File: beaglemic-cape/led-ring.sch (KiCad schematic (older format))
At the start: 42 parts, among them U1 74HC595, U2 74HC595, U3 AMS1117

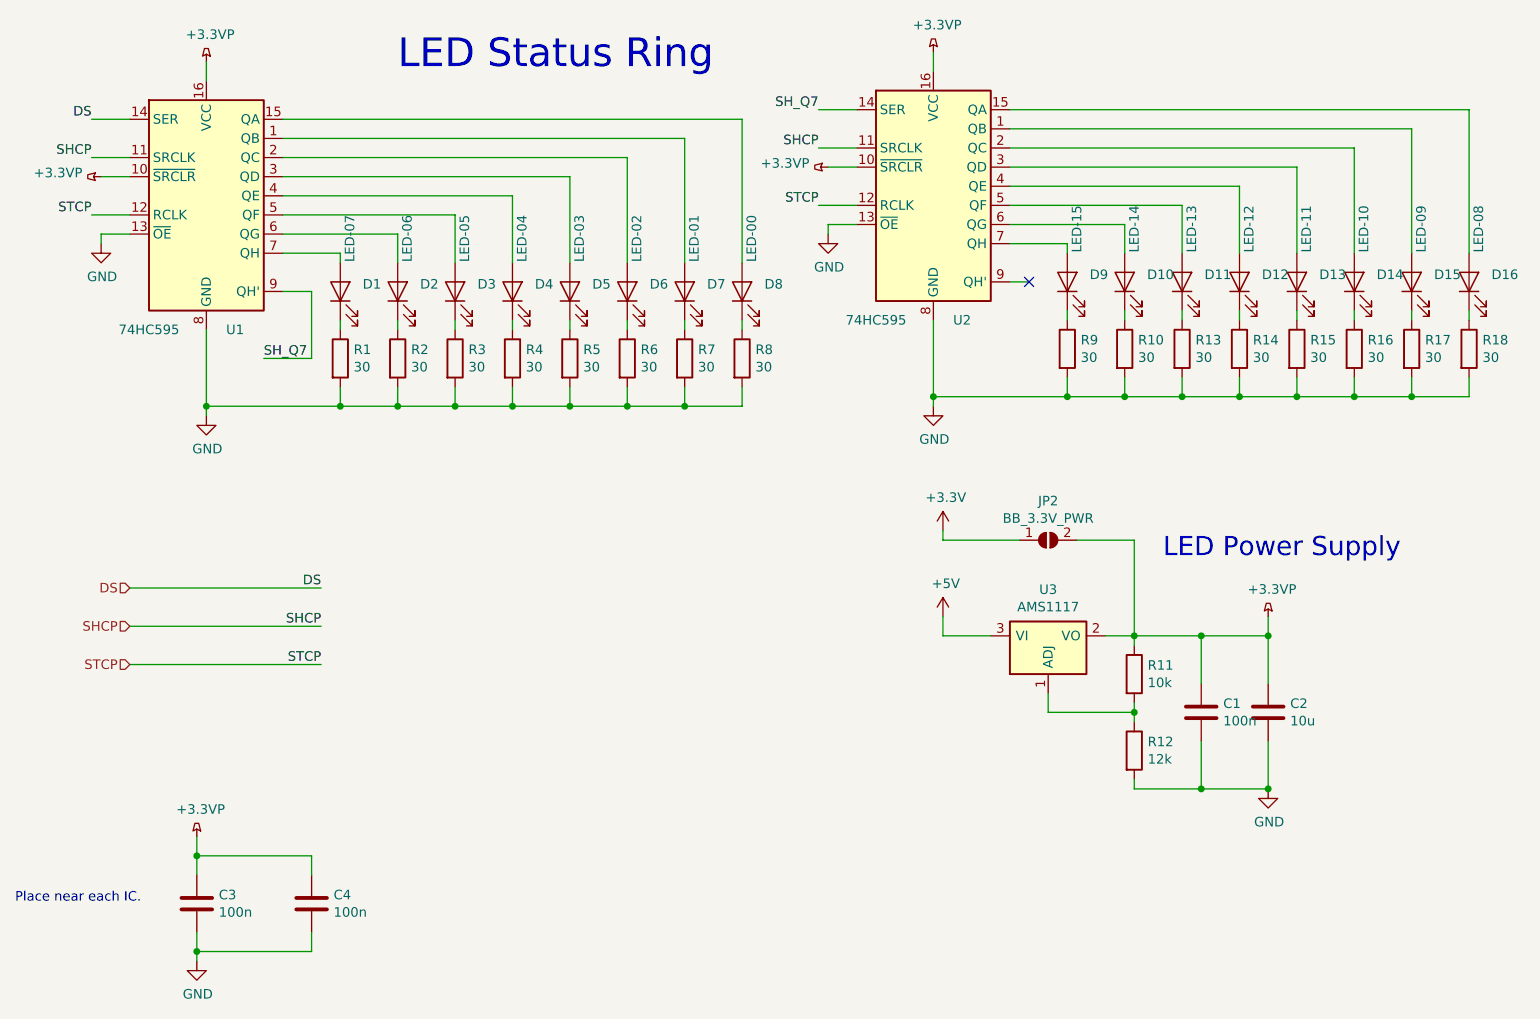
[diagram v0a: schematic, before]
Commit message: beaglemic-cape: Shrink PCB to 100x100mm
Let's keep the PCB in the hobby price range.

Version 1.0-rc2

TODO: Route me!

Signed-off-by: Dimitar Dimitrov <dimitar@dinux.eu>
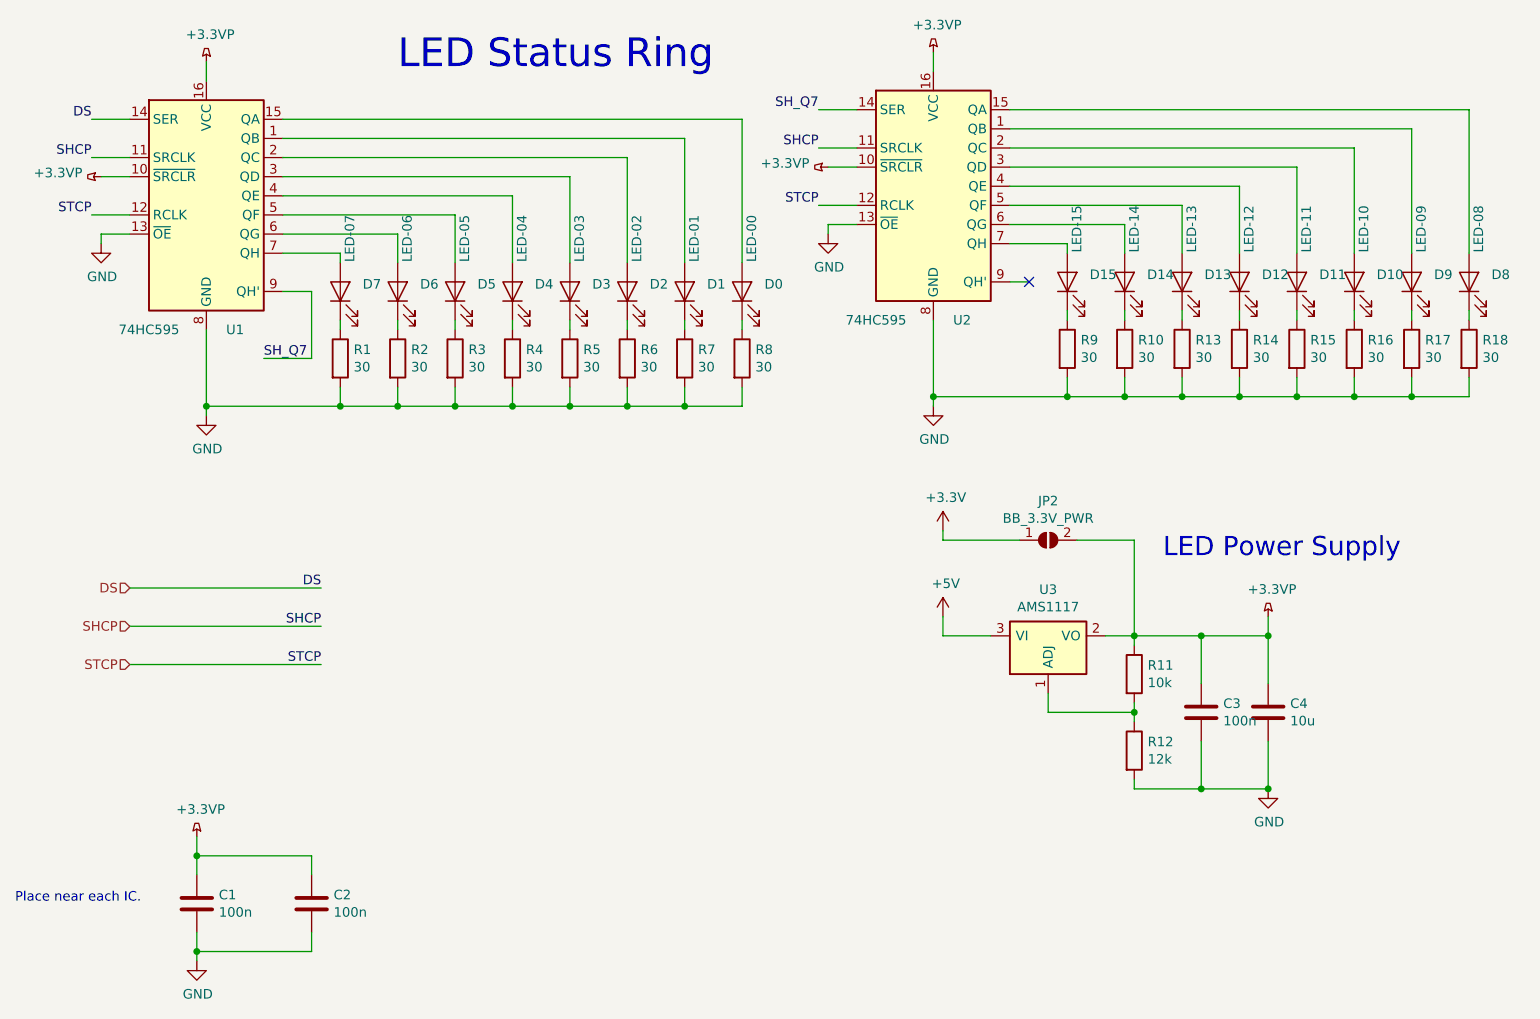
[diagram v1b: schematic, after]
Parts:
- renumbered C3 to C1, C4 to C2, C1 to C3, C2 to C4, D8 to D0, D7 to D1, D14 to D10, D13 to D11, D11 to D13, D10 to D14, D9 to D15, D6 to D2, D5 to D3, D3 to D5, D2 to D6, D1 to D7, D16 to D8, D15 to D9
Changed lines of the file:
@@
 Sheet 2 3
 Title "LED Ring"
-Date "2020-01-04"
-Rev "1.0-rc1"
+Date "2020-01-19"
+Rev "1.0-rc2"
 Comp "dimitar@dinux.eu"
 Comment1 "WARNING - NOT YET VALIDATED!"
@@
 $EndComp
 $Comp
-L power:GND #PWR046
+L power:GND #PWR049
 U 1 1 5E16CB08
 P 7650 5050
-F 0 "#PWR046" H 7650 4800 50  0001 C CNN
+F 0 "#PWR049" H 7650 4800 50  0001 C CNN
 F 1 "GND" H 7655 4877 50  0000 C CNN
 F 2 "" H 7650 5050 50  0001 C CNN
@@
 $EndComp
 $Comp
-L power:+3.3VP #PWR045
+L power:+3.3VP #PWR048
 U 1 1 5E16CB0E
 P 7650 4150
-F 0 "#PWR045" H 7800 4100 50  0001 C CNN
+F 0 "#PWR048" H 7800 4100 50  0001 C CNN
 F 1 "+3.3VP" H 7670 4293 50  0000 C CNN
 F 2 "" H 7650 4150 50  0001 C CNN
@@
 $EndComp
 $Comp
-L power:+5V #PWR044
+L power:+5V #PWR047
 U 1 1 5E16CB14
 P 5950 4150
-F 0 "#PWR044" H 5950 4000 50  0001 C CNN
+F 0 "#PWR047" H 5950 4000 50  0001 C CNN
 F 1 "+5V" H 5965 4323 50  0000 C CNN
 F 2 "" H 5950 4150 50  0001 C CNN
@@
 $EndComp
 $Comp
-L power:+3.3V #PWR043
+L power:+3.3V #PWR046
 U 1 1 5E16CB1A
 P 5950 3700
-F 0 "#PWR043" H 5950 3550 50  0001 C CNN
+F 0 "#PWR046" H 5950 3550 50  0001 C CNN
 F 1 "+3.3V" H 5965 3873 50  0000 C CNN
 F 2 "" H 5950 3700 50  0001 C CNN
@@
 	6950 4650 6950 4700
 $Comp
-L power:+3.3VP #PWR037
+L power:+3.3VP #PWR040
 U 1 1 5E16CB2E
 P 2100 1250
-F 0 "#PWR037" H 2250 1200 50  0001 C CNN
+F 0 "#PWR040" H 2250 1200 50  0001 C CNN
 F 1 "+3.3VP" H 2120 1393 50  0000 C CNN
 F 2 "" H 2100 1250 50  0001 C CNN
@@
 $EndComp
 $Comp
-L power:GND #PWR038
+L power:GND #PWR041
 U 1 1 5E16CB34
 P 2100 3100
-F 0 "#PWR038" H 2100 2850 50  0001 C CNN
+F 0 "#PWR041" H 2100 2850 50  0001 C CNN
 F 1 "GND" H 2105 2927 50  0000 C CNN
 F 2 "" H 2100 3100 50  0001 C CNN
@@
 $EndComp
 $Comp
-L power:+3.3VP #PWR035
+L power:+3.3VP #PWR036
 U 1 1 5E16CB3A
 P 1550 1850
-F 0 "#PWR035" H 1700 1800 50  0001 C CNN
+F 0 "#PWR036" H 1700 1800 50  0001 C CNN
 F 1 "+3.3VP" V 1570 1948 50  0000 L CNN
 F 2 "" H 1550 1850 50  0001 C CNN
@@
 $EndComp
 $Comp
-L power:GND #PWR036
+L power:GND #PWR037
 U 1 1 5E16CB40
 P 1550 2200
-F 0 "#PWR036" H 1550 1950 50  0001 C CNN
+F 0 "#PWR037" H 1550 1950 50  0001 C CNN
 F 1 "GND" H 1555 2027 50  0000 C CNN
 F 2 "" H 1550 2200 50  0001 C CNN
@@
 P 3400 2450
 AR Path="/5E16CB5E" Ref="D?"  Part="1"
-AR Path="/5E0F7674/5E16CB5E" Ref="D3"  Part="1"
-F 0 "D3" V 3438 2333 50  0000 R CNN
+AR Path="/5E0F7674/5E16CB5E" Ref="D5"  Part="1"
+F 0 "D5" V 3438 2333 50  0000 R CNN
 F 1 "LED-05" H 3800 2400 50  0000 R CNN
 F 2 "LED_SMD:LED_0805_2012Metric" H 3400 2450 50  0001 C CNN
@@
 P 3100 2450
 AR Path="/5E16CB6C" Ref="D?"  Part="1"
-AR Path="/5E0F7674/5E16CB6C" Ref="D2"  Part="1"
-F 0 "D2" V 3138 2333 50  0000 R CNN
+AR Path="/5E0F7674/5E16CB6C" Ref="D6"  Part="1"
+F 0 "D6" V 3138 2333 50  0000 R CNN
 F 1 "LED-06" H 3500 2400 50  0000 R CNN
 F 2 "LED_SMD:LED_0805_2012Metric" H 3100 2450 50  0001 C CNN
@@
 P 2800 2450
 AR Path="/5E16CB7A" Ref="D?"  Part="1"
-AR Path="/5E0F7674/5E16CB7A" Ref="D1"  Part="1"
-F 0 "D1" V 2838 2333 50  0000 R CNN
+AR Path="/5E0F7674/5E16CB7A" Ref="D7"  Part="1"
+F 0 "D7" V 2838 2333 50  0000 R CNN
 F 1 "LED-07" H 3200 2400 50  0000 R CNN
 F 2 "LED_SMD:LED_0805_2012Metric" H 2800 2450 50  0001 C CNN
@@
 P 4900 2450
 AR Path="/5E16CB88" Ref="D?"  Part="1"
-AR Path="/5E0F7674/5E16CB88" Ref="D8"  Part="1"
-F 0 "D8" V 4938 2333 50  0000 R CNN
+AR Path="/5E0F7674/5E16CB88" Ref="D0"  Part="1"
+F 0 "D0" V 4938 2333 50  0000 R CNN
 F 1 "LED-00" H 5300 2400 50  0000 R CNN
 F 2 "LED_SMD:LED_0805_2012Metric" H 4900 2450 50  0001 C CNN
@@
 P 4600 2450
 AR Path="/5E16CB96" Ref="D?"  Part="1"
-AR Path="/5E0F7674/5E16CB96" Ref="D7"  Part="1"
-F 0 "D7" V 4638 2333 50  0000 R CNN
+AR Path="/5E0F7674/5E16CB96" Ref="D1"  Part="1"
+F 0 "D1" V 4638 2333 50  0000 R CNN
 F 1 "LED-01" H 5000 2400 50  0000 R CNN
 F 2 "LED_SMD:LED_0805_2012Metric" H 4600 2450 50  0001 C CNN
@@
 P 4300 2450
 AR Path="/5E16CBA4" Ref="D?"  Part="1"
-AR Path="/5E0F7674/5E16CBA4" Ref="D6"  Part="1"
-F 0 "D6" V 4338 2333 50  0000 R CNN
+AR Path="/5E0F7674/5E16CBA4" Ref="D2"  Part="1"
+F 0 "D2" V 4338 2333 50  0000 R CNN
 F 1 "LED-02" H 4700 2400 50  0000 R CNN
 F 2 "LED_SMD:LED_0805_2012Metric" H 4300 2450 50  0001 C CNN
@@
 P 4000 2450
 AR Path="/5E16CBB2" Ref="D?"  Part="1"
-AR Path="/5E0F7674/5E16CBB2" Ref="D5"  Part="1"
-F 0 "D5" V 4038 2333 50  0000 R CNN
+AR Path="/5E0F7674/5E16CBB2" Ref="D3"  Part="1"
+F 0 "D3" V 4038 2333 50  0000 R CNN
 F 1 "LED-03" H 4400 2400 50  0000 R CNN
 F 2 "LED_SMD:LED_0805_2012Metric" H 4000 2450 50  0001 C CNN
@@
 $EndComp
 $Comp
-L power:+3.3VP #PWR041
+L power:+3.3VP #PWR044
 U 1 1 5E16CBFD
 P 5900 1200
-F 0 "#PWR041" H 6050 1150 50  0001 C CNN
+F 0 "#PWR044" H 6050 1150 50  0001 C CNN
 F 1 "+3.3VP" H 5920 1343 50  0000 C CNN
 F 2 "" H 5900 1200 50  0001 C CNN
@@
 $EndComp
 $Comp
-L power:GND #PWR042
+L power:GND #PWR045
 U 1 1 5E16CC03
 P 5900 3050
-F 0 "#PWR042" H 5900 2800 50  0001 C CNN
+F 0 "#PWR045" H 5900 2800 50  0001 C CNN
 F 1 "GND" H 5905 2877 50  0000 C CNN
 F 2 "" H 5900 3050 50  0001 C CNN
@@
 $EndComp
 $Comp
-L power:+3.3VP #PWR039
+L power:+3.3VP #PWR042
 U 1 1 5E16CC09
 P 5350 1800
-F 0 "#PWR039" H 5500 1750 50  0001 C CNN
+F 0 "#PWR042" H 5500 1750 50  0001 C CNN
 F 1 "+3.3VP" V 5370 1898 50  0000 L CNN
 F 2 "" H 5350 1800 50  0001 C CNN
@@
 $EndComp
 $Comp
-L power:GND #PWR040
+L power:GND #PWR043
 U 1 1 5E16CC0F
 P 5350 2150
-F 0 "#PWR040" H 5350 1900 50  0001 C CNN
+F 0 "#PWR043" H 5350 1900 50  0001 C CNN
 F 1 "GND" H 5355 1977 50  0000 C CNN
 F 2 "" H 5350 2150 50  0001 C CNN
@@
 P 7200 2400
 AR Path="/5E16CC2D" Ref="D?"  Part="1"
-AR Path="/5E0F7674/5E16CC2D" Ref="D11"  Part="1"
-F 0 "D11" V 7238 2283 50  0000 R CNN
+AR Path="/5E0F7674/5E16CC2D" Ref="D13"  Part="1"
+F 0 "D13" V 7238 2283 50  0000 R CNN
 F 1 "LED-13" H 7600 2350 50  0000 R CNN
 F 2 "LED_SMD:LED_0805_2012Metric" H 7200 2400 50  0001 C CNN
@@
 P 6900 2400
 AR Path="/5E16CC3B" Ref="D?"  Part="1"
-AR Path="/5E0F7674/5E16CC3B" Ref="D10"  Part="1"
-F 0 "D10" V 6938 2283 50  0000 R CNN
+AR Path="/5E0F7674/5E16CC3B" Ref="D14"  Part="1"
+F 0 "D14" V 6938 2283 50  0000 R CNN
 F 1 "LED-14" H 7300 2350 50  0000 R CNN
 F 2 "LED_SMD:LED_0805_2012Metric" H 6900 2400 50  0001 C CNN
@@
 P 6600 2400
 AR Path="/5E16CC49" Ref="D?"  Part="1"
-AR Path="/5E0F7674/5E16CC49" Ref="D9"  Part="1"
-F 0 "D9" V 6638 2283 50  0000 R CNN
+AR Path="/5E0F7674/5E16CC49" Ref="D15"  Part="1"
+F 0 "D15" V 6638 2283 50  0000 R CNN
 F 1 "LED-15" H 7000 2350 50  0000 R CNN
 F 2 "LED_SMD:LED_0805_2012Metric" H 6600 2400 50  0001 C CNN
@@
 P 8700 2400
 AR Path="/5E16CC57" Ref="D?"  Part="1"
-AR Path="/5E0F7674/5E16CC57" Ref="D16"  Part="1"
-F 0 "D16" V 8738 2283 50  0000 R CNN
+AR Path="/5E0F7674/5E16CC57" Ref="D8"  Part="1"
+F 0 "D8" V 8738 2283 50  0000 R CNN
 F 1 "LED-08" H 9100 2350 50  0000 R CNN
 F 2 "LED_SMD:LED_0805_2012Metric" H 8700 2400 50  0001 C CNN
@@
 P 8400 2400
 AR Path="/5E16CC65" Ref="D?"  Part="1"
-AR Path="/5E0F7674/5E16CC65" Ref="D15"  Part="1"
-F 0 "D15" V 8438 2283 50  0000 R CNN
+AR Path="/5E0F7674/5E16CC65" Ref="D9"  Part="1"
+F 0 "D9" V 8438 2283 50  0000 R CNN
 F 1 "LED-09" H 8800 2350 50  0000 R CNN
 F 2 "LED_SMD:LED_0805_2012Metric" H 8400 2400 50  0001 C CNN
@@
 P 8100 2400
 AR Path="/5E16CC73" Ref="D?"  Part="1"
-AR Path="/5E0F7674/5E16CC73" Ref="D14"  Part="1"
-F 0 "D14" V 8138 2283 50  0000 R CNN
+AR Path="/5E0F7674/5E16CC73" Ref="D10"  Part="1"
+F 0 "D10" V 8138 2283 50  0000 R CNN
 F 1 "LED-10" H 8500 2350 50  0000 R CNN
 F 2 "LED_SMD:LED_0805_2012Metric" H 8100 2400 50  0001 C CNN
@@
 P 7800 2400
 AR Path="/5E16CC81" Ref="D?"  Part="1"
-AR Path="/5E0F7674/5E16CC81" Ref="D13"  Part="1"
-F 0 "D13" V 7838 2283 50  0000 R CNN
+AR Path="/5E0F7674/5E16CC81" Ref="D11"  Part="1"
+F 0 "D11" V 7838 2283 50  0000 R CNN
 F 1 "LED-11" H 8200 2350 50  0000 R CNN
 F 2 "LED_SMD:LED_0805_2012Metric" H 7800 2400 50  0001 C CNN
@@
 NoConn ~ 6400 2400
 $Comp
-L Device:C C1
+L Device:C C3
 U 1 1 5E16CCC3
 P 7300 4650
-F 0 "C1" H 7415 4696 50  0000 L CNN
+F 0 "C3" H 7415 4696 50  0000 L CNN
 F 1 "100n" H 7415 4605 50  0000 L CNN
 F 2 "Capacitor_SMD:C_0805_2012Metric" H 7338 4500 50  0001 C CNN
@@
 $EndComp
 $Comp
-L Device:C C2
+L Device:C C4
 U 1 1 5E16CCCA
 P 7650 4650
-F 0 "C2" H 7765 4696 50  0000 L CNN
+F 0 "C4" H 7765 4696 50  0000 L CNN
 F 1 "10u" H 7765 4605 50  0000 L CNN
 F 2 "Capacitor_SMD:C_0805_2012Metric" H 7688 4500 50  0001 C CNN
@@
 STCP
 $Comp
-L Device:C C3
+L Device:C C1
 U 1 1 5E1C7255
 P 2050 5650
-F 0 "C3" H 2165 5696 50  0000 L CNN
+F 0 "C1" H 2165 5696 50  0000 L CNN
 F 1 "100n" H 2165 5605 50  0000 L CNN
 F 2 "Capacitor_SMD:C_0805_2012Metric" H 2088 5500 50  0001 C CNN
@@
 $EndComp
 $Comp
-L power:+3.3VP #PWR0101
+L power:+3.3VP #PWR038
 U 1 1 5E1C7325
 P 2050 5300
-F 0 "#PWR0101" H 2200 5250 50  0001 C CNN
+F 0 "#PWR038" H 2200 5250 50  0001 C CNN
 F 1 "+3.3VP" H 2070 5443 50  0000 C CNN
 F 2 "" H 2050 5300 50  0001 C CNN
@@
 $EndComp
 $Comp
-L power:GND #PWR0102
+L power:GND #PWR039
 U 1 1 5E1C7382
 P 2050 5950
-F 0 "#PWR0102" H 2050 5700 50  0001 C CNN
+F 0 "#PWR039" H 2050 5700 50  0001 C CNN
 F 1 "GND" H 2055 5777 50  0000 C CNN
 F 2 "" H 2050 5950 50  0001 C CNN
@@
 Place near each IC.
 $Comp
-L Device:C C4
+L Device:C C2
 U 1 1 5E1C74D6
 P 2650 5650
-F 0 "C4" H 2765 5696 50  0000 L CNN
+F 0 "C2" H 2765 5696 50  0000 L CNN
 F 1 "100n" H 2765 5605 50  0000 L CNN
 F 2 "Capacitor_SMD:C_0805_2012Metric" H 2688 5500 50  0001 C CNN

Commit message: beaglemic-cape: Minor documentation updates
Signed-off-by: Dimitar Dimitrov <dimitar@dinux.eu>
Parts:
- R12: value 12k -> 12k**
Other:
- note added: "** Change to 0 Ohm\nif using AMS1117-3.3"
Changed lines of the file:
@@
 Sheet 2 3
 Title "LED Ring"
-Date "2020-01-26"
-Rev "1.0-rc3"
+Date "2020-04-05"
+Rev "1.0-rc4"
 Comp "dimitar@dinux.eu"
 Comment1 "WARNING - NOT YET VALIDATED!"
@@
 AR Path="/5E0F7674/5E16CB01" Ref="R12"  Part="1"
 F 0 "R12" H 7020 4896 50  0000 L CNN
-F 1 "12k" H 7020 4805 50  0000 L CNN
+F 1 "12k**" H 7020 4805 50  0000 L CNN
 F 2 "Resistor_SMD:R_0805_2012Metric" V 6880 4850 50  0001 C CNN
 F 3 "~" H 6950 4850 50  0001 C CNN
@@
 Wire Wire Line
 	2050 5900 2050 5950
+Text Notes 5850 5450 0    100  Italic 0
+** Change to 0 Ohm\nif using AMS1117-3.3
 $EndSCHEMATC
